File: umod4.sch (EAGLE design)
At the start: 101 parts, among them IC1 27C256-FEED-THRU, M1 Generic single-sided NEO-8, M2 RPi Pico W, Q1 DNP/SI2301CDS, Q2 SS8050, U1 RP2040, U2 W25Q128JVSIQ, U3 SY6280AAC, U4 74LVC2G04, U5 74LVC541, U6 74LVC541, U7 74LVC4245, U8 TLV75733P, Y1 12MHz

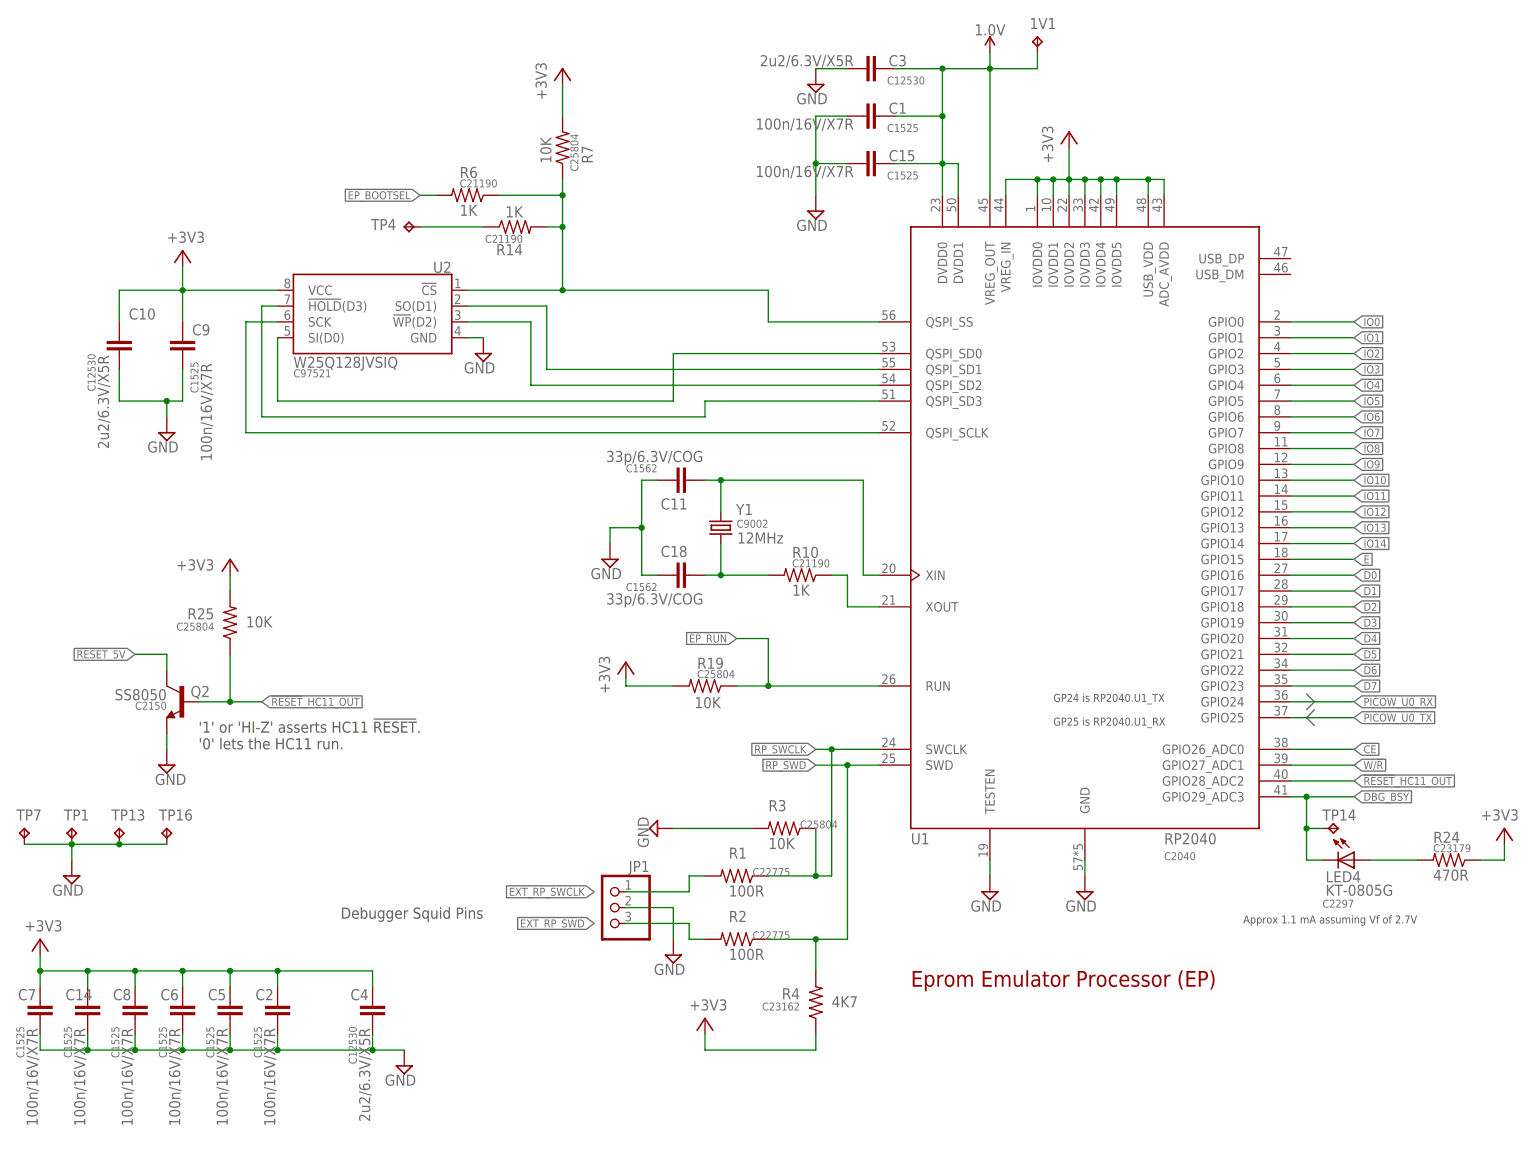
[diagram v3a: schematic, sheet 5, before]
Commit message: Replace all 100nF 0402 packages with SMD-0402-NOM
- Affected parts: C1, C2, C5, C6, C7, C8, C9, C12, C14, C15, C19, C20, C22, C25, C27, C28
- LCSC_PART unchanged
- Manually reworked wire angles on board to clear DRC failures from the new pad geometry
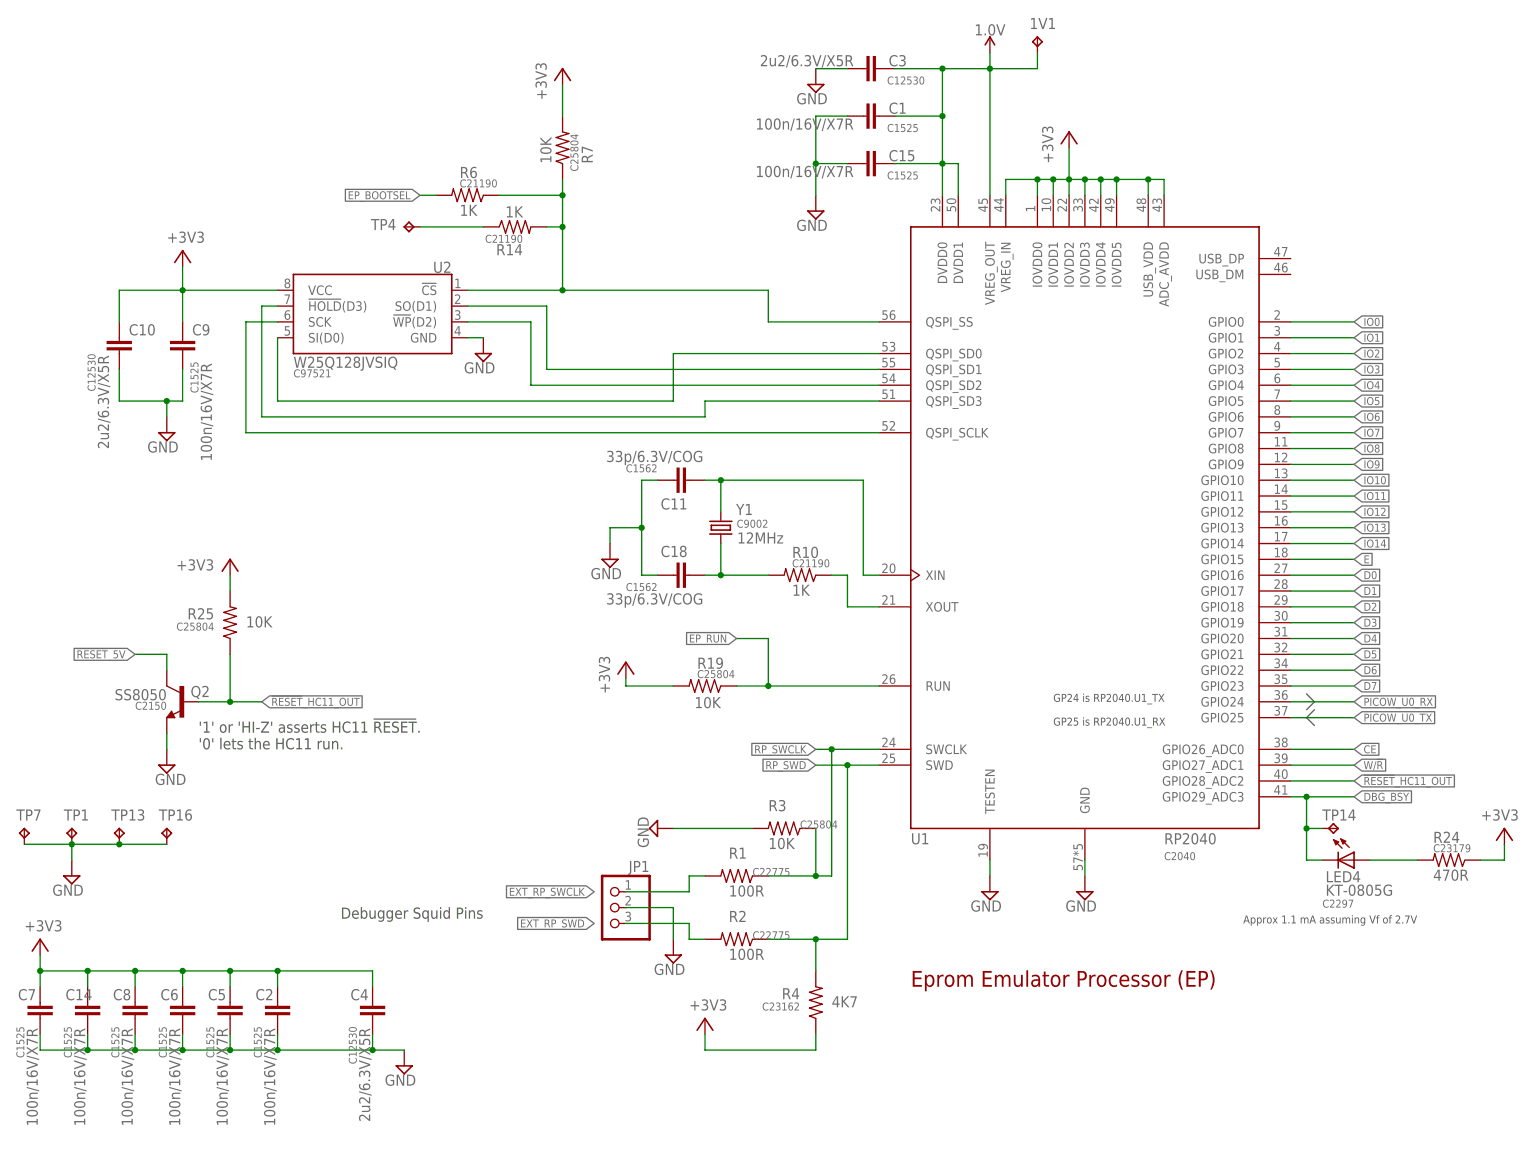
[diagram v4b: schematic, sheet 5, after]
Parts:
- C1, C12, C14, C15, C19, C2, C20, C22, C25, C27, C28, C5, C6, C7, C8, C9: device SparkFun-03-01-2010:CAP0402-CAP -> robins-v7:CAP-0402-NOM

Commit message: Replace all 10uF 0805 packages with SMD-0805-NOM
- Affected parts: C16, C17, C24
- LCSC_PART unchanged
- Manually reworked wire angles on board to clear DRC failures from the new pad geometry
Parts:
- C16, C17, C24: device robins-v7:CAP-0805 -> robins-v7:CAP-0805-NOM
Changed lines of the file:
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@@
 </part>
 <part name="TP15" library="robins-v7" deviceset="TEST-POINT" device="-1035" value="1035"/>
-<part name="C24" library="robins-v7" deviceset="CAP" device="-0805" value="10u/25V/X5R">
+<part name="C24" library="robins-v7" deviceset="CAP" device="-0805-NOM" value="10u/25V/X5R">
 <attribute name="LCSC_PART" value="C15850"/>
 </part>
 <part name="V49" library="supply2" deviceset="GND" device=""/>
-<part name="C16" library="robins-v7" deviceset="CAP" device="-0805" value="10u/25V/X5R">
+<part name="C16" library="robins-v7" deviceset="CAP" device="-0805-NOM" value="10u/25V/X5R">
 <attribute name="LCSC_PART" value="C15850"/>
 </part>
-<part name="C17" library="robins-v7" deviceset="CAP" device="-0805" value="10u/25V/X5R">
+<part name="C17" library="robins-v7" deviceset="CAP" device="-0805-NOM" value="10u/25V/X5R">
 <attribute name="LCSC_PART" value="C15850"/>
 </part>

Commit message: Added test point for VDD_SD
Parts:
- added TP17: 1035, robins-v7:TEST-POINT-1035
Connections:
- net VDD_SD: now also TP17.TP
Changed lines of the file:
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@@
 </part>
 <part name="TP16" library="robins-v7" deviceset="TEST-POINT" device="-1035" value="1035"/>
+<part name="TP17" library="robins-v7" deviceset="TEST-POINT" device="-1035" value="1035"/>
 </parts>
 <sheets>
@@
 <attribute name="VALUE" x="42.164" y="84.201" size="1.778" layer="96"/>
 </instance>
+<instance part="TP17" gate="G$1" x="99.06" y="81.28" smashed="yes">
+<attribute name="NAME" x="97.79" y="81.28" size="1.778" layer="95" rot="R90"/>
+</instance>
 </instances>
 <busses>
@@
 <pinref part="U3" gate="G$1" pin="OUT"/>
 <label x="104.14" y="76.2" size="1.27" layer="95" xref="yes"/>
-<wire x1="86.36" y1="76.2" x2="104.14" y2="76.2" width="0.1524" layer="91"/>
-</segment>
-</net>
+<wire x1="86.36" y1="76.2" x2="99.06" y2="76.2" width="0.1524" layer="91"/>
+<pinref part="TP17" gate="G$1" pin="TP"/>
+<wire x1="99.06" y1="76.2" x2="104.14" y2="76.2" width="0.1524" layer="91"/>
+<wire x1="99.06" y1="76.2" x2="99.06" y2="81.28" width="0.1524" layer="91"/>
+<junction x="99.06" y="76.2"/>
+</segment>
+</net>
